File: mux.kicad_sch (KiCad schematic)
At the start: 22 parts, among them M1 SN74LV4051ADYYR, M10 SN74LV4051ADYYR, M11 SN74LV4051ADYYR, M2 SN74LV4051ADYYR, M3 SN74LV4051ADYYR, M4 SN74LV4051ADYYR, M5 SN74LV4051ADYYR, M6 SN74LV4051ADYYR, M7 SN74LV4051ADYYR, M8 SN74LV4051ADYYR, M9 SN74LV4051ADYYR

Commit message: fix mux
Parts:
- added C284: 100nF, PCM_JLCPCB:C_0402, symbol PCM_JLCPCB-Capacitors:0402,100nF
- added M1, M12, M13, M14, M15, M16, M17, M18, M19, M20, M21: SN74LV4051APWR, SOP65P640X120-16N:SOP65P640X120-16N, symbol SN74LV4051APWR:SN74LV4051APWR
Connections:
- net +3.3VA: now also C284.1, M1.16 (VCC)
- net GND: now also C284.2, M1.6 (INH), M1.7 (GND_1), M1.8 (GND_2), M15.10 (B), M18.9 (C)
- net K19_OUT: now also M1.5 (Y5)
- net K20_OUT: now also M1.4 (Y7)
- net K21_OUT: now also M1.2 (Y6)
- net K22_OUT: now also M1.1 (Y4)
- net K5_OUT: now also M1.12 (Y3)
- net K6_OUT: now also M1.13 (Y0)
- net K7_OUT: now also M1.14 (Y1)
- net K8_OUT: now also M1.15 (Y2)
- net M1_OUT: now also M1.3 (COM)
- net M_SEL_0: now also M1.11 (A)
- net M_SEL_1: now also M1.10 (B)
- net M_SEL_2: now also M1.9 (C)
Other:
- moved on the sheet: C186, M1

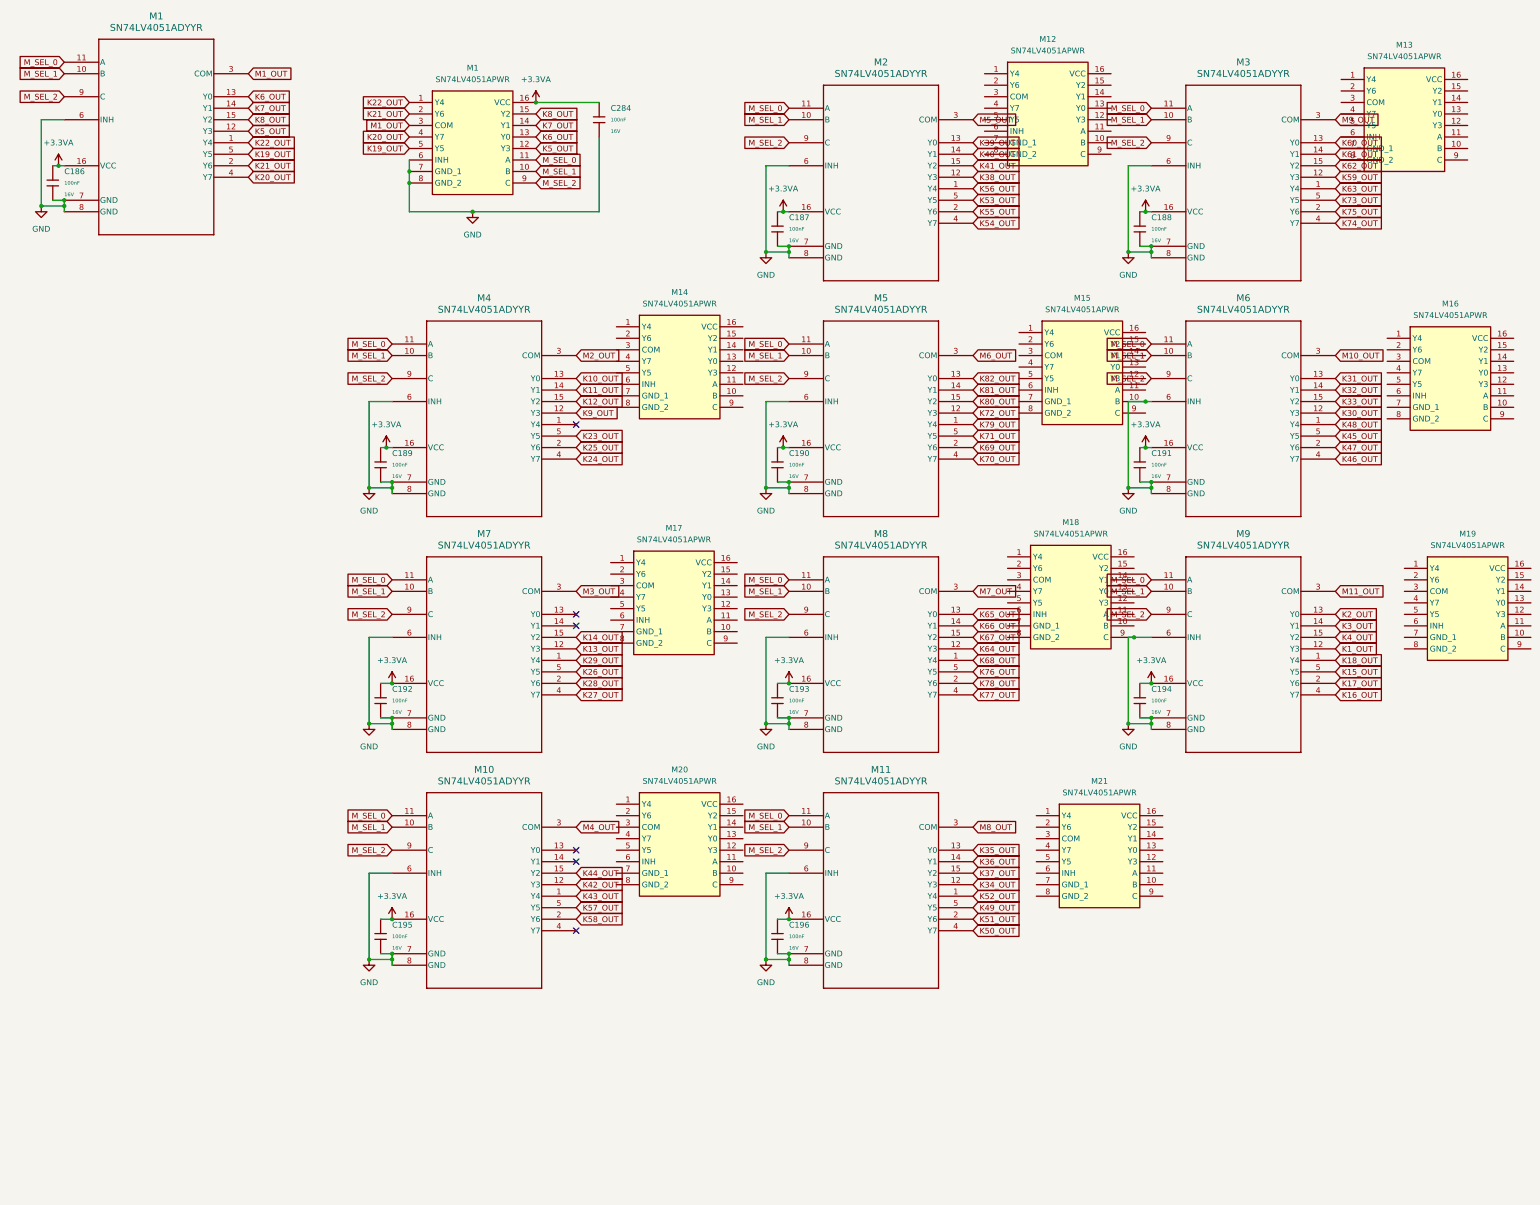
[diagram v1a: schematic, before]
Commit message: replace mux
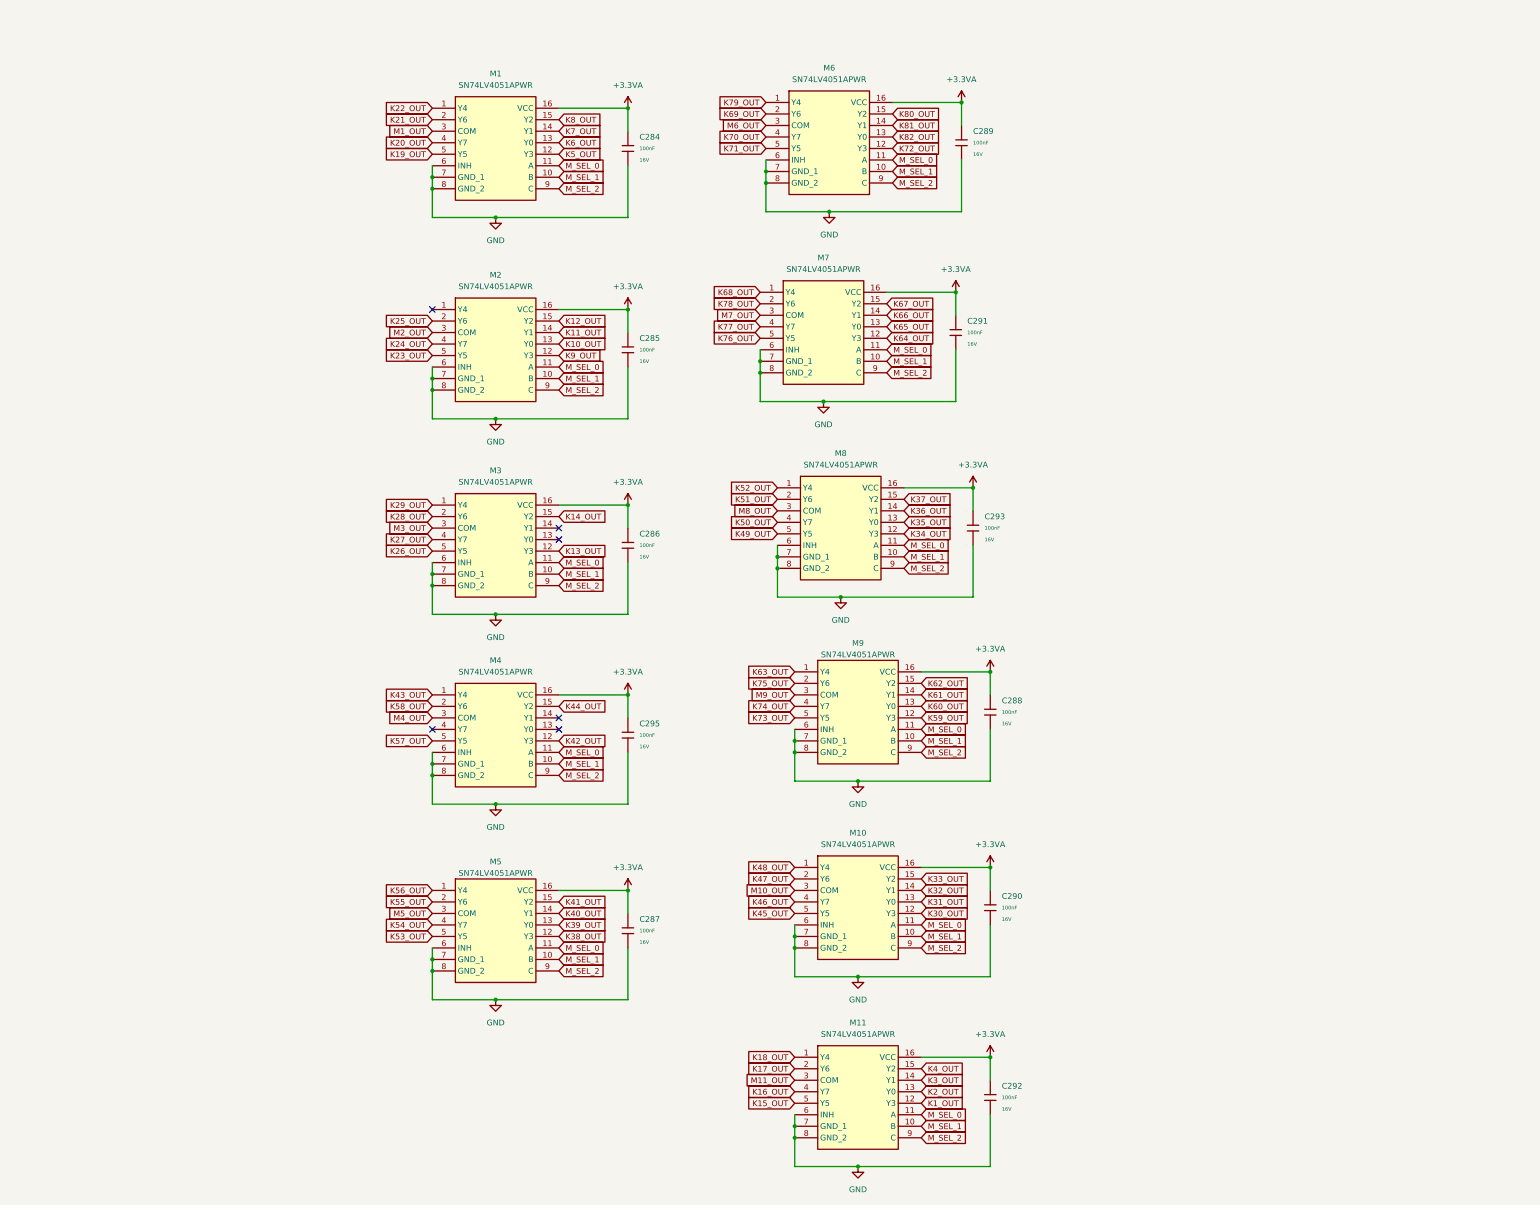
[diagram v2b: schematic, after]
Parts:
- removed C186, C187, C188, C189, C190, C191, C192, C193, C194, C195, C196: 100nF, PCM_JLCPCB:C_0402, symbol PCM_JLCPCB-Capacitors:0402,100nF
- removed M1, M10, M11, M2, M3, M4, M5, M6, M7, M8, M9: SN74LV4051ADYYR, SN74LV4051ADYYR:SOT-23-THIN16_DYY_TEX, symbol SN74LV4051ADYYR:SN74LV4051ADYYR
- removed M12, M13, M14, M15, M16, M17, M18, M19, M20, M21: SN74LV4051APWR, SOP65P640X120-16N:SOP65P640X120-16N, symbol SN74LV4051APWR:SN74LV4051APWR
- added C285, C286, C287, C288, C289, C290, C291, C292, C293, C295: 100nF, PCM_JLCPCB:C_0402, symbol PCM_JLCPCB-Capacitors:0402,100nF
- added M10, M11, M2, M3, M4, M5, M6, M7, M8, M9: SN74LV4051APWR, SOP65P640X120-16N:SOP65P640X120-16N, symbol SN74LV4051APWR:SN74LV4051APWR
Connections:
- net +3.3VA: now also C285.1, C286.1, C287.1, C288.1, C289.1, C290.1, C291.1, C292.1, C293.1, C295.1, M10.16 (VCC), M11.16 (VCC), M2.16 (VCC), M3.16 (VCC), M4.16 (VCC), M5.16 (VCC), M6.16 (VCC), M7.16 (VCC), M8.16 (VCC), M9.16 (VCC)
- net GND: now also C285.2, C286.2, C287.2, C288.2, C289.2, C290.2, C291.2, C292.2, C293.2, C295.2, M10.6 (INH), M10.7 (GND_1), M10.8 (GND_2), M11.6 (INH), M11.7 (GND_1), M11.8 (GND_2), M2.6 (INH), M2.7 (GND_1), M2.8 (GND_2), M3.6 (INH), M3.7 (GND_1), M3.8 (GND_2), M4.6 (INH), M4.7 (GND_1), M4.8 (GND_2), M5.6 (INH), M5.7 (GND_1), M5.8 (GND_2), M6.6 (INH), M6.7 (GND_1), M6.8 (GND_2), M7.6 (INH), M7.7 (GND_1), M7.8 (GND_2), M8.6 (INH), M8.7 (GND_1), M8.8 (GND_2), M9.6 (INH), M9.7 (GND_1), M9.8 (GND_2)
- net K10_OUT: now also M2.13 (Y0)
- net K11_OUT: now also M2.14 (Y1)
- net K12_OUT: now also M2.15 (Y2)
- net K13_OUT: now also M3.12 (Y3)
- net K14_OUT: now also M3.15 (Y2)
- net K15_OUT: now also M11.5 (Y5)
- net K16_OUT: now also M11.4 (Y7)
- net K17_OUT: now also M11.2 (Y6)
- net K18_OUT: now also M11.1 (Y4)
- net K1_OUT: now also M11.12 (Y3)
- net K23_OUT: now also M2.5 (Y5)
- net K24_OUT: now also M2.4 (Y7)
- net K25_OUT: now also M2.2 (Y6)
- net K26_OUT: now also M3.5 (Y5)
- net K27_OUT: now also M3.4 (Y7)
- net K28_OUT: now also M3.2 (Y6)
- net K29_OUT: now also M3.1 (Y4)
- net K2_OUT: now also M11.13 (Y0)
- net K30_OUT: now also M10.12 (Y3)
- net K31_OUT: now also M10.13 (Y0)
- net K32_OUT: now also M10.14 (Y1)
- net K33_OUT: now also M10.15 (Y2)
- net K34_OUT: now also M8.12 (Y3)
- net K35_OUT: now also M8.13 (Y0)
- net K36_OUT: now also M8.14 (Y1)
- net K37_OUT: now also M8.15 (Y2)
- net K38_OUT: now also M5.12 (Y3)
- net K39_OUT: now also M5.13 (Y0)
- net K3_OUT: now also M11.14 (Y1)
- net K40_OUT: now also M5.14 (Y1)
- net K41_OUT: now also M5.15 (Y2)
- net K42_OUT: now also M4.12 (Y3)
- net K43_OUT: now also M4.1 (Y4)
- net K44_OUT: now also M4.15 (Y2)
- net K45_OUT: now also M10.5 (Y5)
- net K46_OUT: now also M10.4 (Y7)
- net K47_OUT: now also M10.2 (Y6)
- net K48_OUT: now also M10.1 (Y4)
- net K49_OUT: now also M8.5 (Y5)
- net K4_OUT: now also M11.15 (Y2)
- net K50_OUT: now also M8.4 (Y7)
- net K51_OUT: now also M8.2 (Y6)
- net K52_OUT: now also M8.1 (Y4)
- net K53_OUT: now also M5.5 (Y5)
- net K54_OUT: now also M5.4 (Y7)
- net K55_OUT: now also M5.2 (Y6)
- net K56_OUT: now also M5.1 (Y4)
- net K57_OUT: now also M4.5 (Y5)
- net K58_OUT: now also M4.2 (Y6)
- net K59_OUT: now also M9.12 (Y3)
- net K60_OUT: now also M9.13 (Y0)
- net K61_OUT: now also M9.14 (Y1)
- net K62_OUT: now also M9.15 (Y2)
- net K63_OUT: now also M9.1 (Y4)
- net K64_OUT: now also M7.12 (Y3)
- net K65_OUT: now also M7.13 (Y0)
- net K66_OUT: now also M7.14 (Y1)
- net K67_OUT: now also M7.15 (Y2)
- net K68_OUT: now also M7.1 (Y4)
- net K69_OUT: now also M6.2 (Y6)
- net K70_OUT: now also M6.4 (Y7)
- net K71_OUT: now also M6.5 (Y5)
- net K72_OUT: now also M6.12 (Y3)
- net K73_OUT: now also M9.5 (Y5)
- net K74_OUT: now also M9.4 (Y7)
- net K75_OUT: now also M9.2 (Y6)
- net K76_OUT: now also M7.5 (Y5)
- net K77_OUT: now also M7.4 (Y7)
- net K78_OUT: now also M7.2 (Y6)
- net K79_OUT: now also M6.1 (Y4)
- net K80_OUT: now also M6.15 (Y2)
- net K81_OUT: now also M6.14 (Y1)
- net K82_OUT: now also M6.13 (Y0)
- net K9_OUT: now also M2.12 (Y3)
- net M10_OUT: now also M10.3 (COM)
- net M11_OUT: now also M11.3 (COM)
- net M2_OUT: now also M2.3 (COM)
- net M3_OUT: now also M3.3 (COM)
- net M4_OUT: now also M4.3 (COM)
- net M5_OUT: now also M5.3 (COM)
- net M6_OUT: now also M6.3 (COM)
- net M7_OUT: now also M7.3 (COM)
- net M8_OUT: now also M8.3 (COM)
- net M9_OUT: now also M9.3 (COM)
- net M_SEL_0: now also M10.11 (A), M11.11 (A), M2.11 (A), M3.11 (A), M4.11 (A), M5.11 (A), M6.11 (A), M7.11 (A), M8.11 (A), M9.11 (A)
- net M_SEL_1: now also M10.10 (B), M11.10 (B), M2.10 (B), M3.10 (B), M4.10 (B), M5.10 (B), M6.10 (B), M7.10 (B), M8.10 (B), M9.10 (B)
- net M_SEL_2: now also M10.9 (C), M11.9 (C), M2.9 (C), M3.9 (C), M4.9 (C), M5.9 (C), M6.9 (C), M7.9 (C), M8.9 (C), M9.9 (C)
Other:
- moved on the sheet: C284, M1

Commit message: latest
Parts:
- M1, M10, M11, M2, M3, M4, M5, M6, M7, M8, M9: LCSC (none) -> C7793
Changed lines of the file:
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@@
 			)
 		)
+		(property "LCSC" "C7793"
+			(at 38.1 158.75 0)
+			(hide yes)
+			(show_name no)
+			(do_not_autoplace no)
+			(effects
+				(font
+					(size 1.27 1.27)
+				)
+			)
+		)
 		(pin "7"
 		)
@@
 			)
 		)
+		(property "LCSC" "C7793"
+			(at 38.1 116.84 0)
+			(hide yes)
+			(show_name no)
+			(do_not_autoplace no)
+			(effects
+				(font
+					(size 1.27 1.27)
+				)
+			)
+		)
 		(pin "7"
 		)
@@
 			)
 		)
+		(property "LCSC" "C7793"
+			(at 118.11 238.76 0)
+			(hide yes)
+			(show_name no)
+			(do_not_autoplace no)
+			(effects
+				(font
+					(size 1.27 1.27)
+				)
+			)
+		)
 		(pin "7"
 		)
@@
 			)
 		)
+		(property "LCSC" "C7793"
+			(at 118.11 196.85 0)
+			(hide yes)
+			(show_name no)
+			(do_not_autoplace no)
+			(effects
+				(font
+					(size 1.27 1.27)
+				)
+			)
+		)
 		(pin "7"
 		)
@@
 			)
 		)
+		(property "LCSC" "C7793"
+			(at 111.76 27.94 0)
+			(hide yes)
+			(show_name no)
+			(do_not_autoplace no)
+			(effects
+				(font
+					(size 1.27 1.27)
+				)
+			)
+		)
 		(pin "7"
 		)
@@
 			)
 		)
+		(property "LCSC" "C7793"
+			(at 38.1 201.93 0)
+			(hide yes)
+			(show_name no)
+			(do_not_autoplace no)
+			(effects
+				(font
+					(size 1.27 1.27)
+				)
+			)
+		)
 		(pin "7"
 		)
@@
 			)
 		)
+		(property "LCSC" "C7793"
+			(at 38.1 73.66 0)
+			(hide yes)
+			(show_name no)
+			(do_not_autoplace no)
+			(effects
+				(font
+					(size 1.27 1.27)
+				)
+			)
+		)
 		(pin "7"
 		)
@@
 			)
 		)
+		(property "LCSC" "C7793"
+			(at 110.49 69.85 0)
+			(hide yes)
+			(show_name no)
+			(do_not_autoplace no)
+			(effects
+				(font
+					(size 1.27 1.27)
+				)
+			)
+		)
 		(pin "7"
 		)
@@
 			)
 		)
+		(property "LCSC" "C7793"
+			(at 38.1 29.21 0)
+			(hide yes)
+			(show_name no)
+			(do_not_autoplace no)
+			(effects
+				(font
+					(size 1.27 1.27)
+				)
+			)
+		)
 		(pin "7"
 		)
@@
 			)
 		)
+		(property "LCSC" "C7793"
+			(at 118.11 153.67 0)
+			(hide yes)
+			(show_name no)
+			(do_not_autoplace no)
+			(effects
+				(font
+					(size 1.27 1.27)
+				)
+			)
+		)
 		(pin "7"
 		)
@@
 			)
 		)
+		(property "LCSC" "C7793"
+			(at 114.3 113.03 0)
+			(hide yes)
+			(show_name no)
+			(do_not_autoplace no)
+			(effects
+				(font
+					(size 1.27 1.27)
+				)
+			)
+		)

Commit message: Reorganize KiCad libraries; add Legacy Docs
Large repository reorganization of KiCad assets: added Docs and Legacy/ proto directories with many component datasheets and legacy project files, moved and renamed numerous footprints, 3D models and symbol files into consolidated Library/ and Legacy/ paths, and removed outdated/duplicate files. Purpose is to centralize libraries, preserve legacy designs, and clean up footprint/3D model locations for easier maintenance.
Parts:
- M1, M10, M11, M2, M3, M4, M5, M6, M7, M8, M9: footprint SOP65P640X120-16N:SOP65P640X120-16N -> SN74LV4051APWR:SOP65P640X120-16N
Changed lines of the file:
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@@
 			)
 		)
-		(property "Footprint" "SOP65P640X120-16N:SOP65P640X120-16N"
+		(property "Footprint" "SN74LV4051APWR:SOP65P640X120-16N"
 			(at 62.23 253.67 0)
 			(hide yes)
@@
 			)
 		)
-		(property "Footprint" "SOP65P640X120-16N:SOP65P640X120-16N"
+		(property "Footprint" "SN74LV4051APWR:SOP65P640X120-16N"
 			(at 62.23 211.76 0)
 			(hide yes)
@@
 			)
 		)
-		(property "Footprint" "SOP65P640X120-16N:SOP65P640X120-16N"
+		(property "Footprint" "SN74LV4051APWR:SOP65P640X120-16N"
 			(at 142.24 333.68 0)
 			(hide yes)
@@
 			)
 		)
-		(property "Footprint" "SOP65P640X120-16N:SOP65P640X120-16N"
+		(property "Footprint" "SN74LV4051APWR:SOP65P640X120-16N"
 			(at 142.24 291.77 0)
 			(hide yes)
@@
 			)
 		)
-		(property "Footprint" "SOP65P640X120-16N:SOP65P640X120-16N"
+		(property "Footprint" "SN74LV4051APWR:SOP65P640X120-16N"
 			(at 135.89 122.86 0)
 			(hide yes)
@@
 			)
 		)
-		(property "Footprint" "SOP65P640X120-16N:SOP65P640X120-16N"
+		(property "Footprint" "SN74LV4051APWR:SOP65P640X120-16N"
 			(at 62.23 296.85 0)
 			(hide yes)
@@
 			)
 		)
-		(property "Footprint" "SOP65P640X120-16N:SOP65P640X120-16N"
+		(property "Footprint" "SN74LV4051APWR:SOP65P640X120-16N"
 			(at 62.23 168.58 0)
 			(hide yes)
@@
 			)
 		)
-		(property "Footprint" "SOP65P640X120-16N:SOP65P640X120-16N"
+		(property "Footprint" "SN74LV4051APWR:SOP65P640X120-16N"
 			(at 134.62 164.77 0)
 			(hide yes)
@@
 			)
 		)
-		(property "Footprint" "SOP65P640X120-16N:SOP65P640X120-16N"
+		(property "Footprint" "SN74LV4051APWR:SOP65P640X120-16N"
 			(at 62.23 124.13 0)
 			(hide yes)
@@
 			)
 		)
-		(property "Footprint" "SOP65P640X120-16N:SOP65P640X120-16N"
+		(property "Footprint" "SN74LV4051APWR:SOP65P640X120-16N"
 			(at 142.24 248.59 0)
 			(hide yes)
@@
 			)
 		)
-		(property "Footprint" "SOP65P640X120-16N:SOP65P640X120-16N"
+		(property "Footprint" "SN74LV4051APWR:SOP65P640X120-16N"
 			(at 138.43 207.95 0)
 			(hide yes)
